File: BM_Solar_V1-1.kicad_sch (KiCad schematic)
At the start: 19 parts, among them J1 LiPo, J10 Conn_01x16_Pin, J2 LiFePO4, J4 Batt 1S, J5 Thrm - 10k, J8 Conn_01x16_Pin, J9 Solar 3-18V, U1 BQ25185DLHR

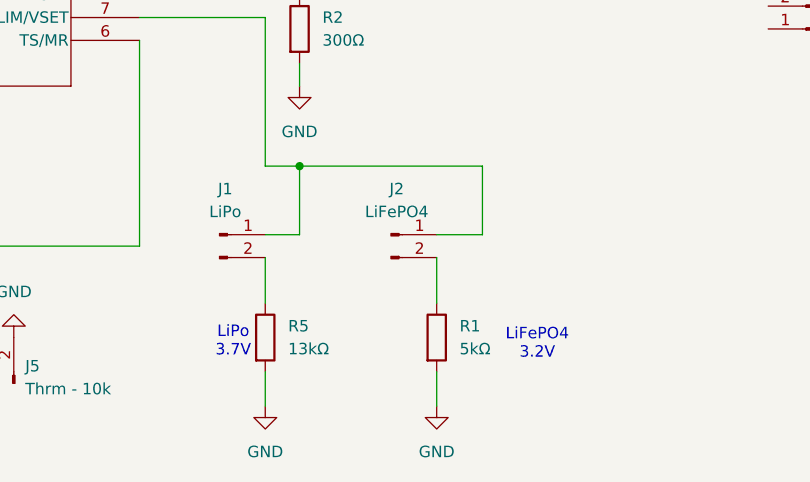
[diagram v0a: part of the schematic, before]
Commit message: Changed to a 1x3 pin header for battery select, rearranged batt sense circuit, improved traces, and added more vias for more thermal dissipation.
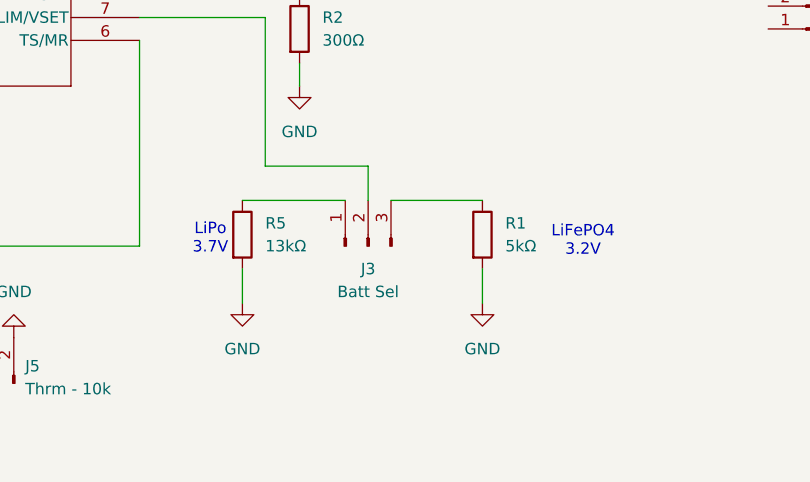
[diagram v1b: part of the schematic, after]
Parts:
- removed J1: LiPo, Connector_PinHeader_2.54mm:PinHeader_1x02_P2.54mm_Vertical, symbol Connector:Conn_01x02_Pin
- removed J2: LiFePO4, Connector_PinHeader_2.54mm:PinHeader_1x02_P2.54mm_Vertical, symbol Connector:Conn_01x02_Pin
- added J3: Batt Sel, Connector_PinHeader_2.54mm:PinHeader_1x03_P2.54mm_Vertical, symbol Connector:Conn_01x03_Pin
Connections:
- net at R5.1: now also J3.1 (Pin_1)
- net at U1.7 (ILIM/VSET): now also J3.2 (Pin_2)
- net at R1.1: now also J3.3 (Pin_3)
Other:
- moved on the sheet: R1, R5
